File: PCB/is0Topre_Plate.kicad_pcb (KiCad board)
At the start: 2 copper layers, 29.3 x 51.1 mm, 3 parts

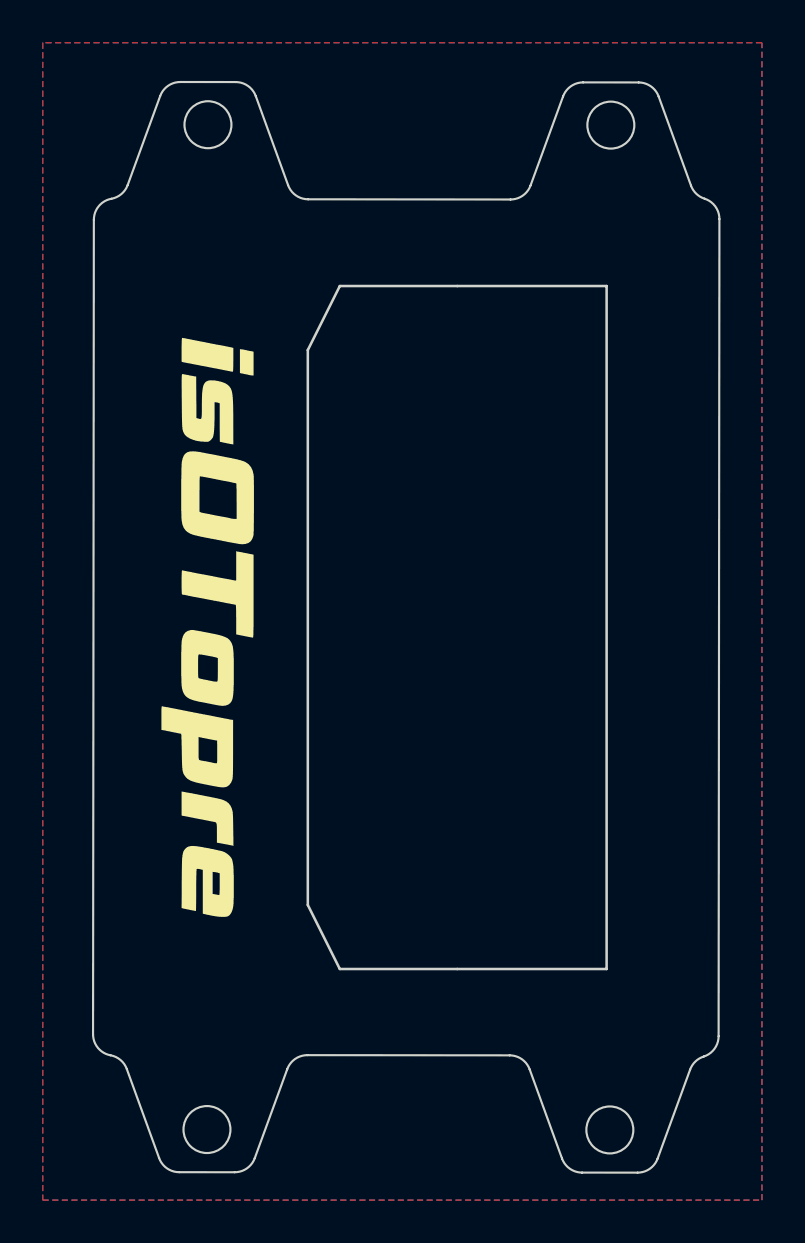
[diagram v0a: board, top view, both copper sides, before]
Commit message: Update to add tape silkscreen
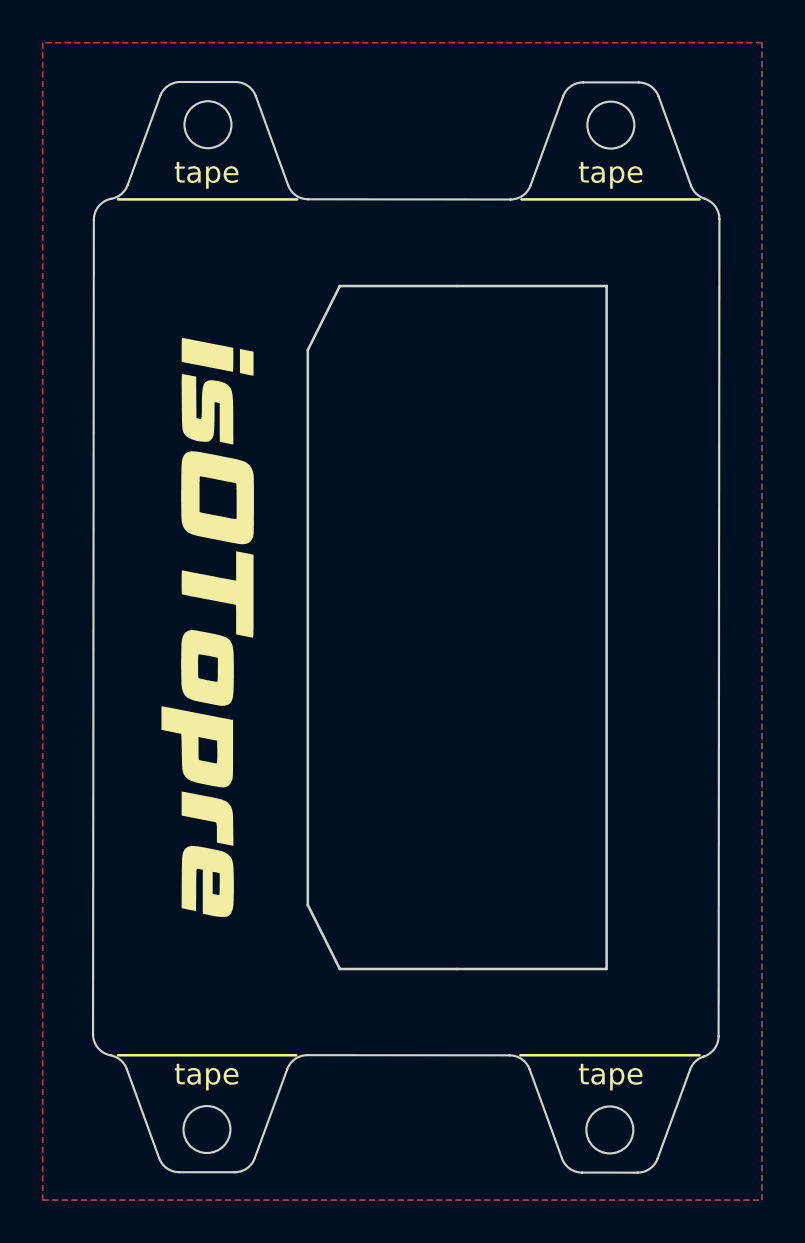
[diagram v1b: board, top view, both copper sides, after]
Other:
- board text added: "tape"
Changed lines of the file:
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@@
       ) (layer "B.SilkS") (width 0.01) (fill solid))
   )
+  (gr_line (start 94.74875 79.73125) (end 86.39875 79.73125) (layer "F.SilkS") (width 0.12))
+  (gr_line (start 105.24875 79.73125) (end 113.64875 79.73125) (layer "F.SilkS") (width 0.12))
+  (gr_line (start 94.79875 39.63125) (end 86.39875 39.63125) (layer "F.SilkS") (width 0.12))
+  (gr_line (start 105.29875 39.63125) (end 113.64875 39.63125) (layer "F.SilkS") (width 0.12))
   (gr_arc (start 107.25199 34.80563) (mid 107.618574 34.328844) (end 108.192331 34.148576) (layer "Edge.Cuts") (width 0.1))
   (gr_arc (start 111.681904 84.574061) (mid 111.315317 85.05084) (end 110.741563 85.231114) (layer "Edge.Cuts") (width 0.1))
@@
     (effects (font (size 1 1) (thickness 0.15)) (justify mirror))
   )
+  (gr_text "tape\n" (at 90.567231 38.38125) (layer "F.SilkS")
+    (effects (font (size 1 1) (thickness 0.15)))
+  )
+  (gr_text "tape\n" (at 90.567231 80.63125) (layer "F.SilkS")
+    (effects (font (size 1 1) (thickness 0.15)))
+  )
+  (gr_text "tape\n" (at 109.49875 80.63125) (layer "F.SilkS")
+    (effects (font (size 1 1) (thickness 0.15)))
+  )
+  (gr_text "tape\n" (at 109.49875 38.38125) (layer "F.SilkS")
+    (effects (font (size 1 1) (thickness 0.15)))
+  )
   (zone (net 0) (net_name "") (layers F&B.Cu) (hatch edge 0.508)
